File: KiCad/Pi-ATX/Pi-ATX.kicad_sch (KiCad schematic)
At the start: 0 parts

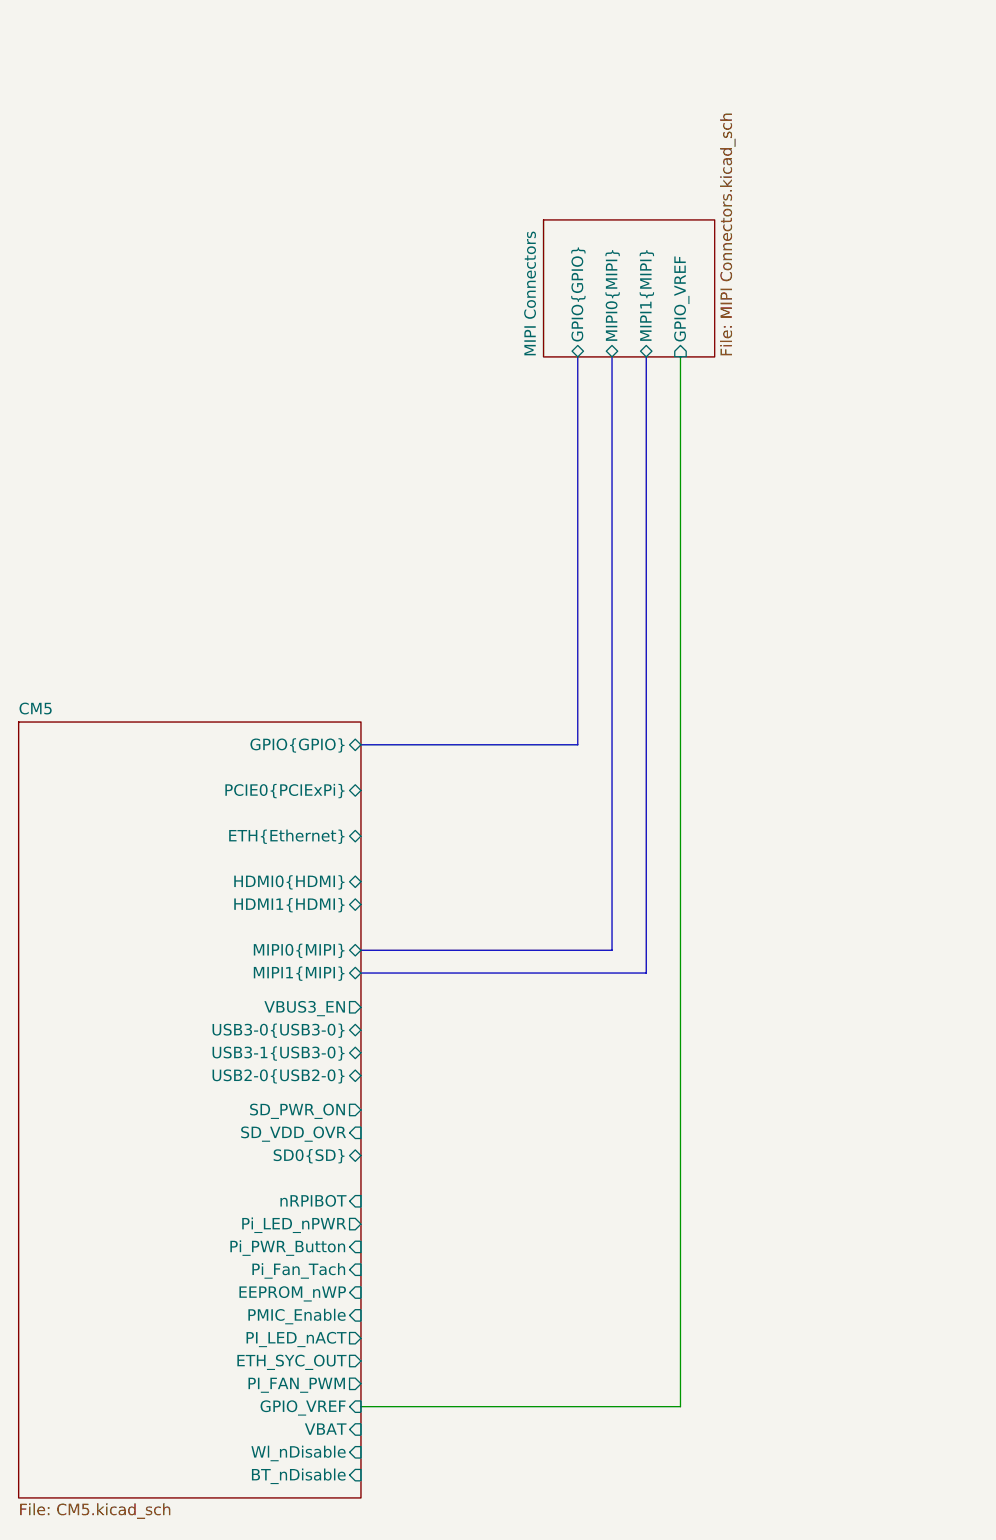
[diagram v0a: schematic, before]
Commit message: added hdmi schematic
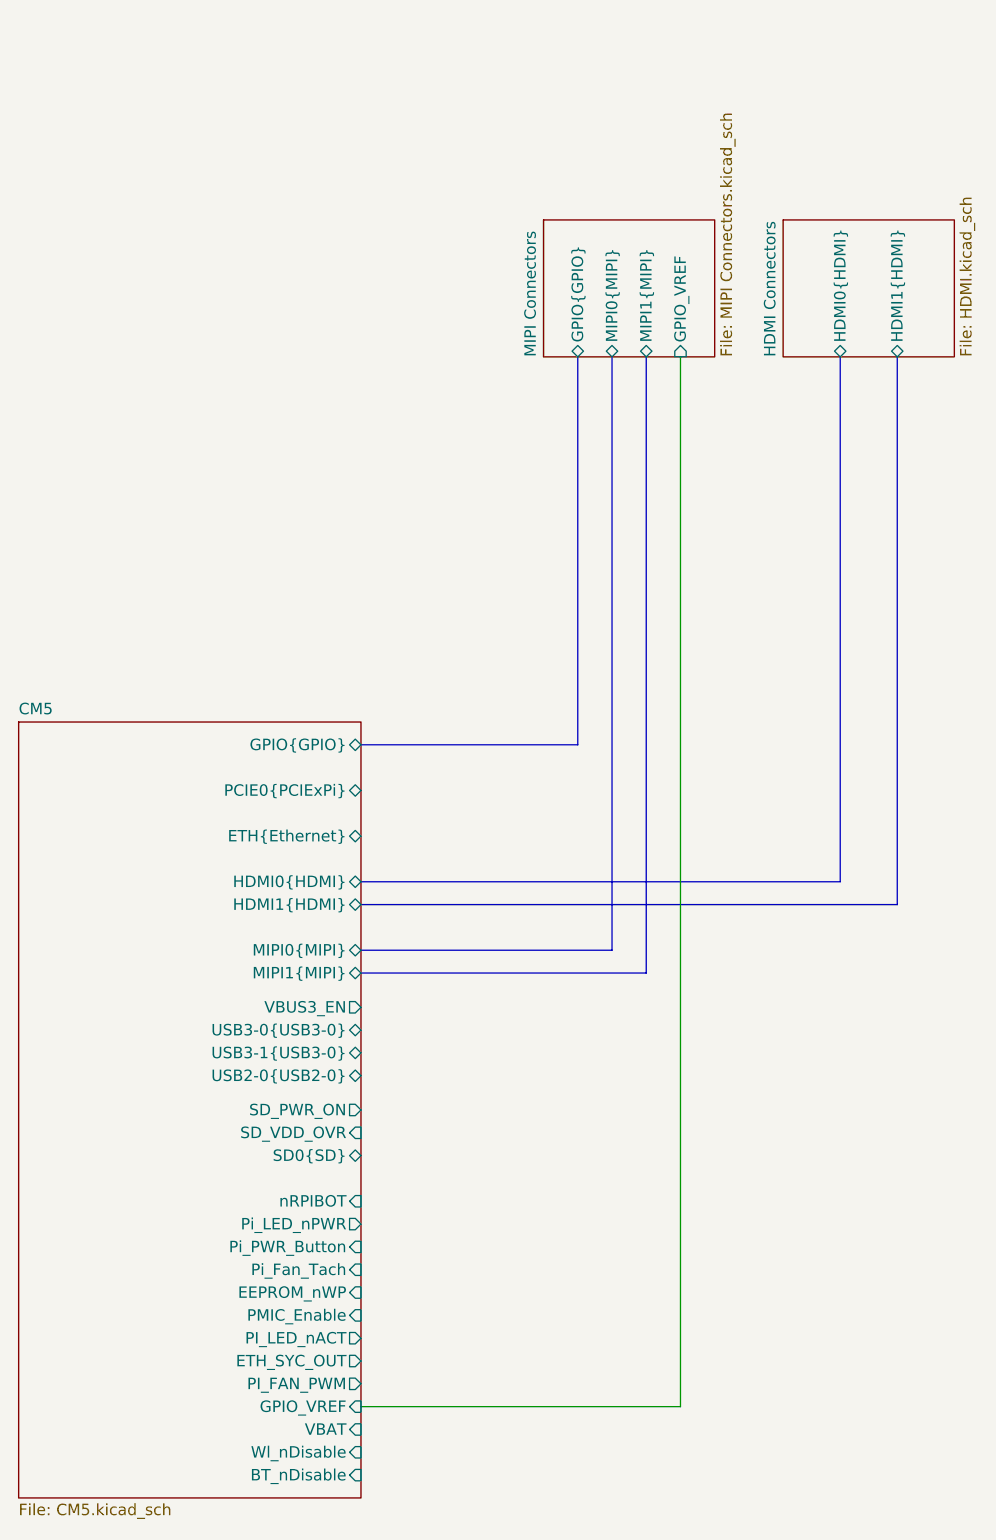
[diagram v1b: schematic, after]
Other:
- added sheet HDMI Connectors (HDMI.kicad_sch)
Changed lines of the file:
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@@
 	(generator_version "9.0")
 	(paper "A4")
+	(bus
+		(pts
+			(xy 53.34 95.25) (xy 113.03 95.25)
+		)
+		(stroke
+			(width 0)
+			(type default)
+		)
+	)
+	(bus
+		(pts
+			(xy 53.34 92.71) (xy 106.68 92.71)
+		)
+		(stroke
+			(width 0)
+			(type default)
+		)
+	)
 	(wire
 		(pts
@@
 		(pts
 			(xy 81.28 100.33) (xy 53.34 100.33)
+		)
+		(stroke
+			(width 0)
+			(type default)
+		)
+	)
+	(bus
+		(pts
+			(xy 106.68 92.71) (xy 106.68 34.29)
 		)
 		(stroke
@@
 	(bus
 		(pts
+			(xy 113.03 95.25) (xy 113.03 34.29)
+		)
+		(stroke
+			(width 0)
+			(type default)
+		)
+	)
+	(bus
+		(pts
 			(xy 53.34 77.47) (xy 77.47 77.47)
 		)
@@
 		)
 	)
+	(sheet
+		(at 100.33 19.05)
+		(size 19.05 15.24)
+		(exclude_from_sim no)
+		(in_bom yes)
+		(on_board yes)
+		(dnp no)
+		(fields_autoplaced yes)
+		(stroke
+			(width 0.1524)
+			(type solid)
+		)
+		(fill
+			(color 0 0 0 0.0000)
+		)
+		(property "Sheetname" "HDMI Connectors"
+			(at 99.6184 34.29 90)
+			(effects
+				(font
+					(size 1.27 1.27)
+				)
+				(justify left bottom)
+			)
+		)
+		(property "Sheetfile" "HDMI.kicad_sch"
+			(at 119.9646 34.29 90)
+			(effects
+				(font
+					(size 1.27 1.27)
+				)
+				(justify left top)
+			)
+		)
+		(pin "HDMI0{HDMI}" bidirectional
+			(at 106.68 34.29 270)
+			(effects
+				(font
+					(size 1.27 1.27)
+				)
+				(justify left)
+			)
+		)
+		(pin "HDMI1{HDMI}" bidirectional
+			(at 113.03 34.29 270)
+			(effects
+				(font
+					(size 1.27 1.27)
+				)
+				(justify left)
+			)
+		)
+		(instances
+			(project "Pi-ATX"
+				(path "/676c920c-f1ce-40bb-8428-0902e451bdf9"
+					(page "4")
+				)
+			)
+		)
+	)
